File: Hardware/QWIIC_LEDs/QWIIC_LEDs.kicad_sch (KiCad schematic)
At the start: 20 parts, among them J1 QWIIC, J3 SWD CONNECTOR, SW1 RST, U2 PY32F030F28U6TR

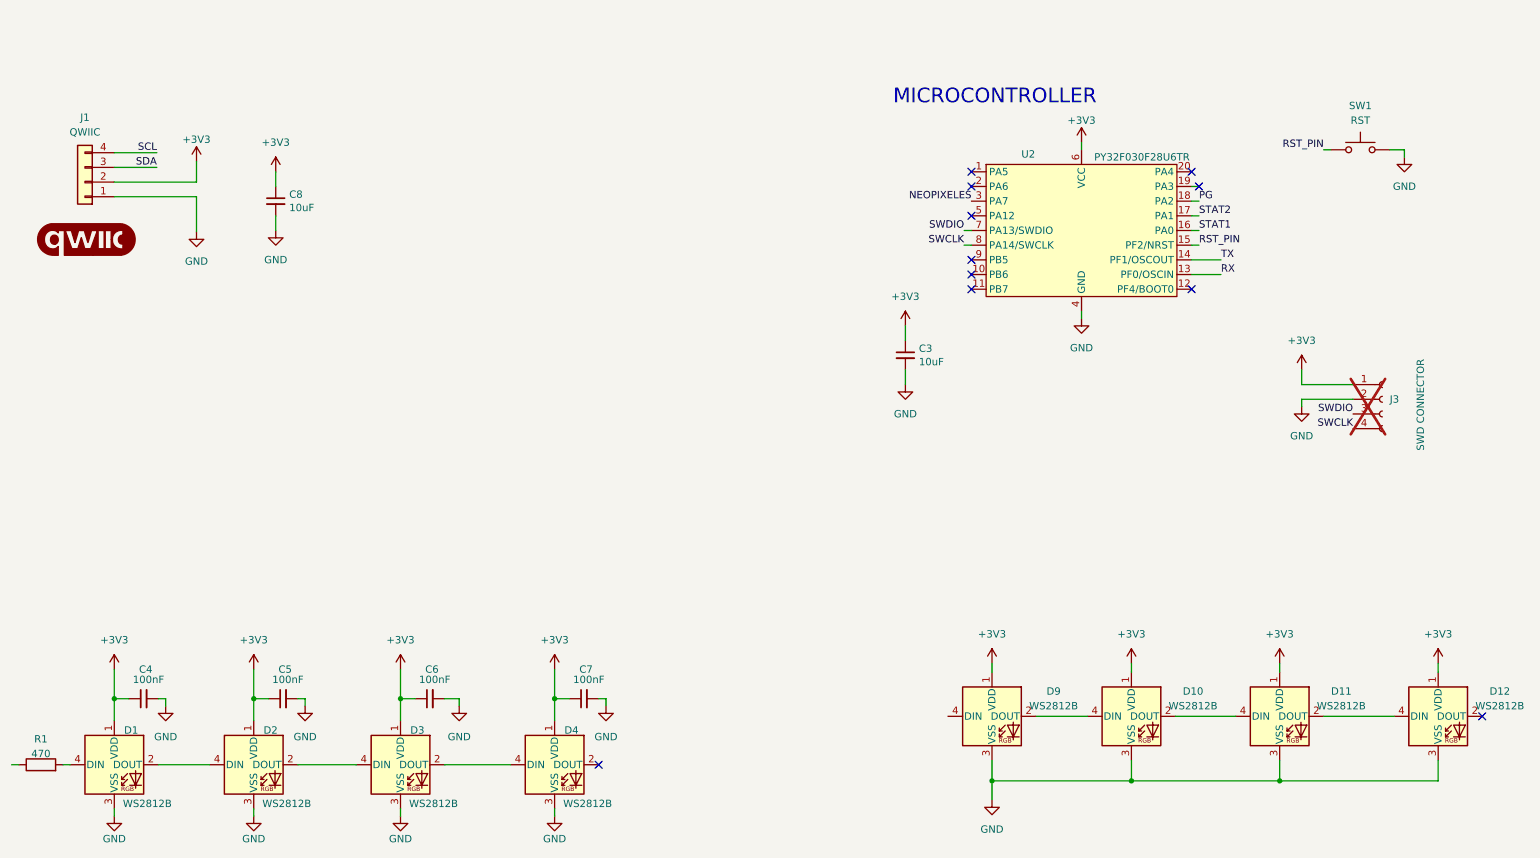
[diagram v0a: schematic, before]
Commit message: Add Qwiic led controller
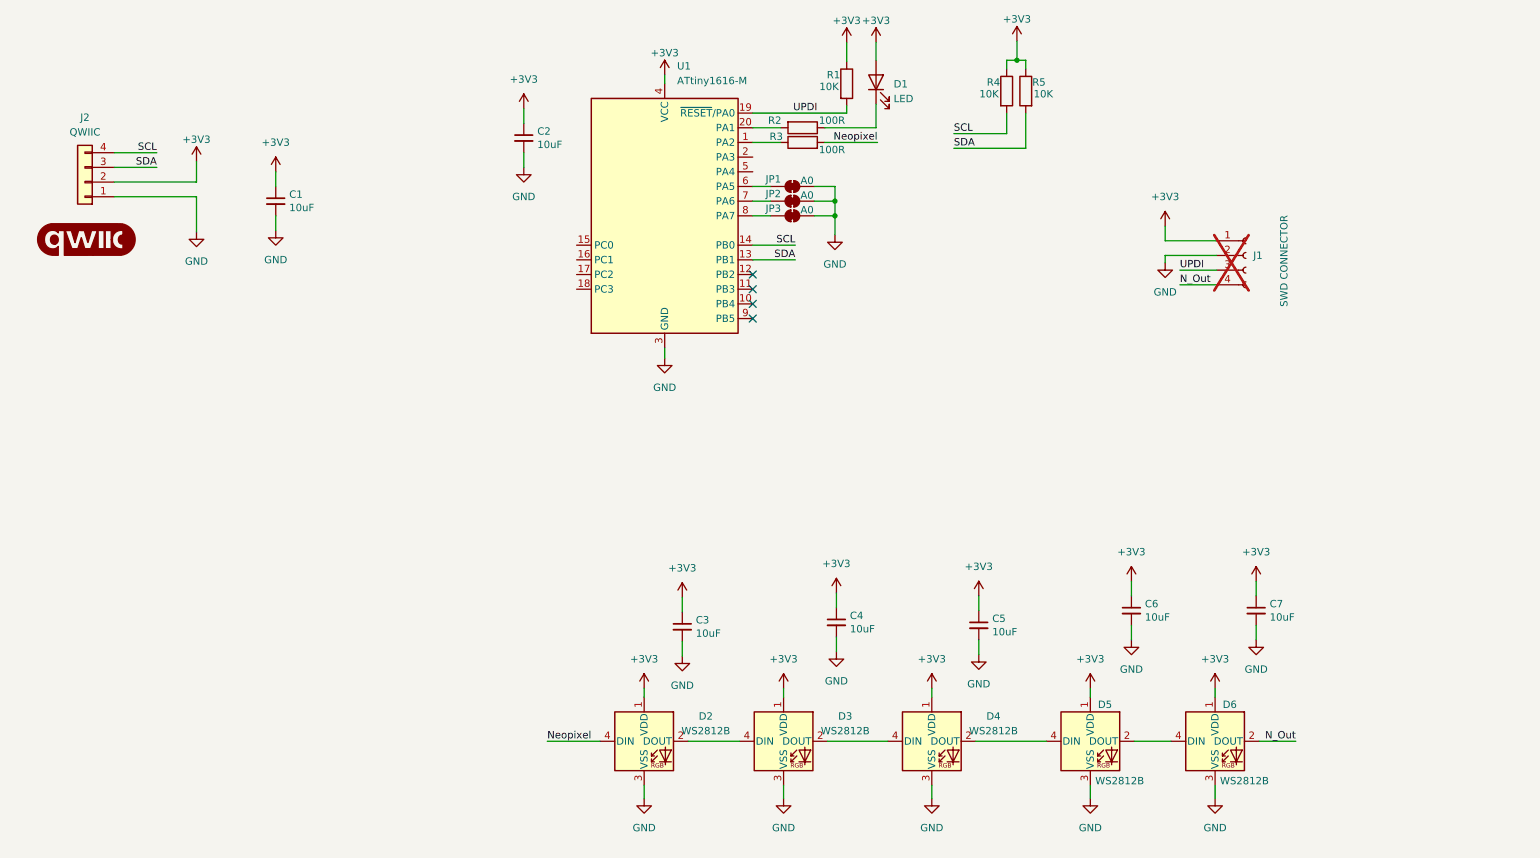
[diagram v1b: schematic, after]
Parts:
- removed D1, D2, D3, D4: WS2812B, LED_SMD:LED_WS2812B-Mini_PLCC4_3.5x3.5mm, symbol LED:WS2812B
- removed SW1: RST, footprints:Button_90, symbol Switch:SW_Push
- removed U2: PY32F030F28U6TR, Package_DFN_QFN:QFN-20-1EP_3x3mm_P0.4mm_EP1.65x1.65mm_ThermalVias, symbol Symbols:PY32F030F2xU
- added C3: 10uF, Capacitor_SMD:C_0603_1608Metric, symbol Device:C_Small
- added D1: LED, LED_SMD:LED_0805_2012Metric_Pad1.15x1.40mm_HandSolder, symbol Device:LED
- added D6: WS2812B, LED_SMD:LED_WS2812B_PLCC4_5.0x5.0mm_P3.2mm, symbol LED:WS2812B
- added JP1, JP2, JP3: A0, Jumper:SolderJumper-2_P1.3mm_Bridged2Bar_RoundedPad1.0x1.5mm, symbol Jumper:SolderJumper_2_Bridged
- added R2, R3: 100R, Resistor_SMD:R_0805_2012Metric, symbol Device:R
- added R4, R5: 10K, Resistor_SMD:R_0805_2012Metric, symbol Device:R
- added U1: ATtiny1616-M, Package_DFN_QFN:VQFN-20-1EP_3x3mm_P0.4mm_EP1.7x1.7mm, symbol MCU_Microchip_ATtiny:ATtiny1616-M
- C4, C5, C6, C7: value 100nF -> 10uF; LCSC# C478888 -> C85713
- J2: renamed from J1; footprint (none) -> SparkFun-Qwiic:JST_SH4
- R1: value 470 -> 10K; footprint Resistor_SMD:R_0603_1608Metric -> Resistor_SMD:R_0805_2012Metric; LCSC# C103661 -> (none); provedor LCSC -> (none)
- renumbered C8 to C1, C3 to C2, D9 to D2, D10 to D3, D11 to D4, D12 to D5, J3 to J1
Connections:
- net SWDIO is gone; now on net UPDI: J1.3 (Pin_3)
- net +3V3: now also R1.1, C3.1, D1.2 (A), D6.1 (VDD), R4.1, R5.1, U1.4 (VCC)
- net GND: now also C3.2, D6.3 (VSS), JP1.2 (B), JP2.2 (B), JP3.2 (B), U1.21 (GND), U1.3 (GND)
- net SCL: now also R4.2, U1.14 (PB0)
- net SDA: now also R5.2, U1.13 (PB1)
- net at D5.2 (DOUT): now also D6.4 (DIN)
- net Neopixel: now reaches D2.4 (DIN)
- net Neopixel: now also R3.2
- net UPDI: now reaches R1.2
- net UPDI: now also U1.19 (~{RESET}/PA0)
- net SWCLK renamed N_Out
- net N_Out: now also D6.2 (DOUT)
- new net: JP3.1 (A), U1.8 (PA7)
- new net: JP2.1 (A), U1.7 (PA6)
- new net: R3.1, U1.1 (PA2)
- new net: R2.2, U1.20 (PA1)
- new net: JP1.1 (A), U1.6 (PA5)
- new net: D1.1 (K), R2.1
- no-connect marks 11 -> 4
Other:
- note removed: "MICROCONTROLLER"
- moved on the sheet: C2, D2, D3, D4, D5, J1
